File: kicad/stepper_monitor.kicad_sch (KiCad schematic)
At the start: 53 parts, among them J1 Conn_01x04_Male, J2 Conn_01x04_Male, J3 Conn_01x02_Male, J4 USB_C_Receptacle_USB2.0, J5 JTAG, M1 Motor-simple_stepper_motor_an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, Q1 UMH3N, Q2 PJA3439, SW1 SW_Push, U1 CP2102N-A01-GQFN28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

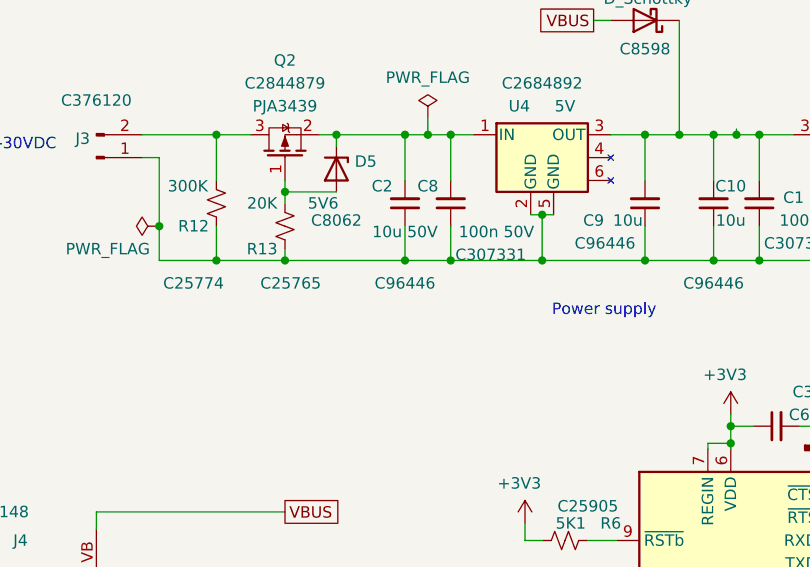
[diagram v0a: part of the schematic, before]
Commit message: Cleaned up the PCB layout.
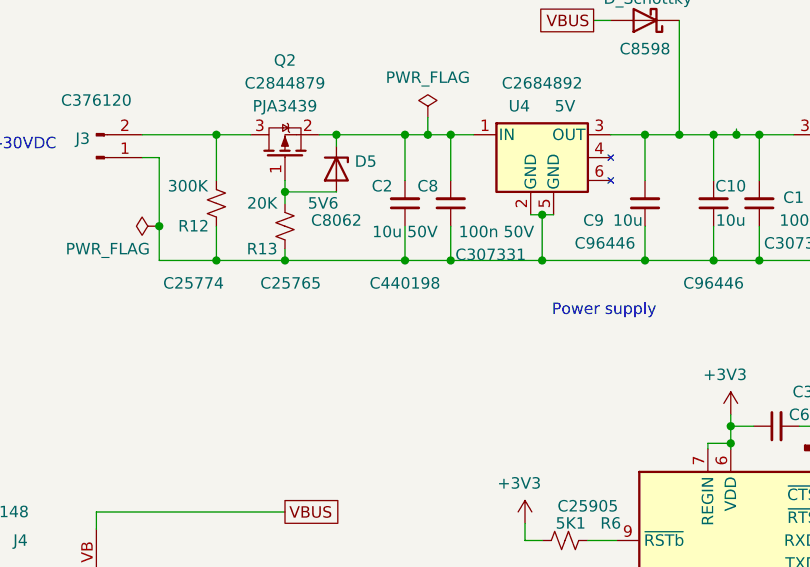
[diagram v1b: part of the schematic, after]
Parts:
- C10, C16, C3, C9: footprint Capacitor_SMD:C_0402_1005Metric -> Capacitor_SMD:C_0603_1608Metric
- C2: footprint Capacitor_SMD:C_0402_1005Metric -> Capacitor_SMD:C_0805_2012Metric; LCSC C96446 -> C440198
- Q2: footprint Package_TO_SOT_SMD:SOT-23 -> stepper_monitor:SOT-23
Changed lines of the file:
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@@
     (property "Reference" "C3" (id 0) (at 126.365 43.18 0))
     (property "Value" "10u" (id 1) (at 126.365 46.99 0))
-    (property "Footprint" "Capacitor_SMD:C_0402_1005Metric" (id 2) (at 128.27 45.085 0)
+    (property "Footprint" "Capacitor_SMD:C_0603_1608Metric" (id 2) (at 128.27 45.085 0)
       (effects (font (size 1.27 1.27)) hide)
     )
@@
     (property "Reference" "C10" (id 0) (at 103.505 43.18 0))
     (property "Value" "10u" (id 1) (at 103.505 46.99 0))
-    (property "Footprint" "Capacitor_SMD:C_0402_1005Metric" (id 2) (at 101.6 45.085 0)
+    (property "Footprint" "Capacitor_SMD:C_0603_1608Metric" (id 2) (at 101.6 45.085 0)
       (effects (font (size 1.27 1.27)) hide)
     )
@@
     (property "Reference" "C2" (id 0) (at 64.77 43.18 0))
     (property "Value" "10u 50V" (id 1) (at 67.31 48.26 0))
-    (property "Footprint" "Capacitor_SMD:C_0402_1005Metric" (id 2) (at 67.31 45.085 0)
+    (property "Footprint" "Capacitor_SMD:C_0805_2012Metric" (id 2) (at 67.31 45.085 0)
       (effects (font (size 1.27 1.27)) hide)
     )
@@
       (effects (font (size 1.27 1.27)) hide)
     )
-    (property "LCSC" "C96446" (id 4) (at 67.31 53.975 0))
+    (property "LCSC" "C440198" (id 4) (at 67.31 53.975 0))
     (pin "1")
     (pin "2")
@@
     (property "Reference" "Q2" (id 0) (at 53.975 29.21 90))
     (property "Value" "PJA3439" (id 1) (at 53.975 34.29 90))
-    (property "Footprint" "Package_TO_SOT_SMD:SOT-23" (id 2) (at 55.88 34.925 0)
+    (property "Footprint" "stepper_monitor:SOT-23" (id 2) (at 55.88 34.925 0)
       (effects (font (size 1.27 1.27) italic) (justify left) hide)
     )
@@
     (property "Reference" "C16" (id 0) (at 205.74 29.845 0))
     (property "Value" "10u" (id 1) (at 205.74 31.75 0))
-    (property "Footprint" "Capacitor_SMD:C_0402_1005Metric" (id 2) (at 209.55 30.48 0)
+    (property "Footprint" "Capacitor_SMD:C_0603_1608Metric" (id 2) (at 209.55 30.48 0)
       (effects (font (size 1.27 1.27)) hide)
     )
@@
     (property "Reference" "C9" (id 0) (at 88.265 46.99 0))
     (property "Value" "10u" (id 1) (at 92.075 46.99 0))
-    (property "Footprint" "Capacitor_SMD:C_0402_1005Metric" (id 2) (at 93.98 45.085 0)
+    (property "Footprint" "Capacitor_SMD:C_0603_1608Metric" (id 2) (at 93.98 45.085 0)
       (effects (font (size 1.27 1.27)) hide)
     )
@@
     )
     (path "/218e73b4-d1ff-4eed-a2d4-42d93c5c0f72"
-      (reference "C2") (unit 1) (value "10u 50V") (footprint "Capacitor_SMD:C_0402_1005Metric")
+      (reference "C2") (unit 1) (value "10u 50V") (footprint "Capacitor_SMD:C_0805_2012Metric")
     )
     (path "/00000000-0000-0000-0000-00006317d8b3"
-      (reference "C3") (unit 1) (value "10u") (footprint "Capacitor_SMD:C_0402_1005Metric")
+      (reference "C3") (unit 1) (value "10u") (footprint "Capacitor_SMD:C_0603_1608Metric")
     )
     (path "/00000000-0000-0000-0000-000063186d0f"
@@
     )
     (path "/cb4273f4-9404-4fd5-bce3-443a59d164e3"
-      (reference "C9") (unit 1) (value "10u") (footprint "Capacitor_SMD:C_0402_1005Metric")
+      (reference "C9") (unit 1) (value "10u") (footprint "Capacitor_SMD:C_0603_1608Metric")
     )
     (path "/093765e9-ac92-428d-96f2-1ae287fc4af6"
-      (reference "C10") (unit 1) (value "10u") (footprint "Capacitor_SMD:C_0402_1005Metric")
+      (reference "C10") (unit 1) (value "10u") (footprint "Capacitor_SMD:C_0603_1608Metric")
     )
     (path "/9ce3787c-7546-4e46-9b55-aaf3ff59b639"
@@
     )
     (path "/bc1a567a-82f7-43c3-b7d6-54c2aa341a86"
-      (reference "C16") (unit 1) (value "10u") (footprint "Capacitor_SMD:C_0402_1005Metric")
+      (reference "C16") (unit 1) (value "10u") (footprint "Capacitor_SMD:C_0603_1608Metric")
     )
     (path "/00000000-0000-0000-0000-00006319144c"
@@
     )
     (path "/420a49fa-bc07-40b0-8b18-684ba9455b7a"
-      (reference "Q2") (unit 1) (value "PJA3439") (footprint "Package_TO_SOT_SMD:SOT-23")
+      (reference "Q2") (unit 1) (value "PJA3439") (footprint "stepper_monitor:SOT-23")
     )
     (path "/00000000-0000-0000-0000-000063145bc1"

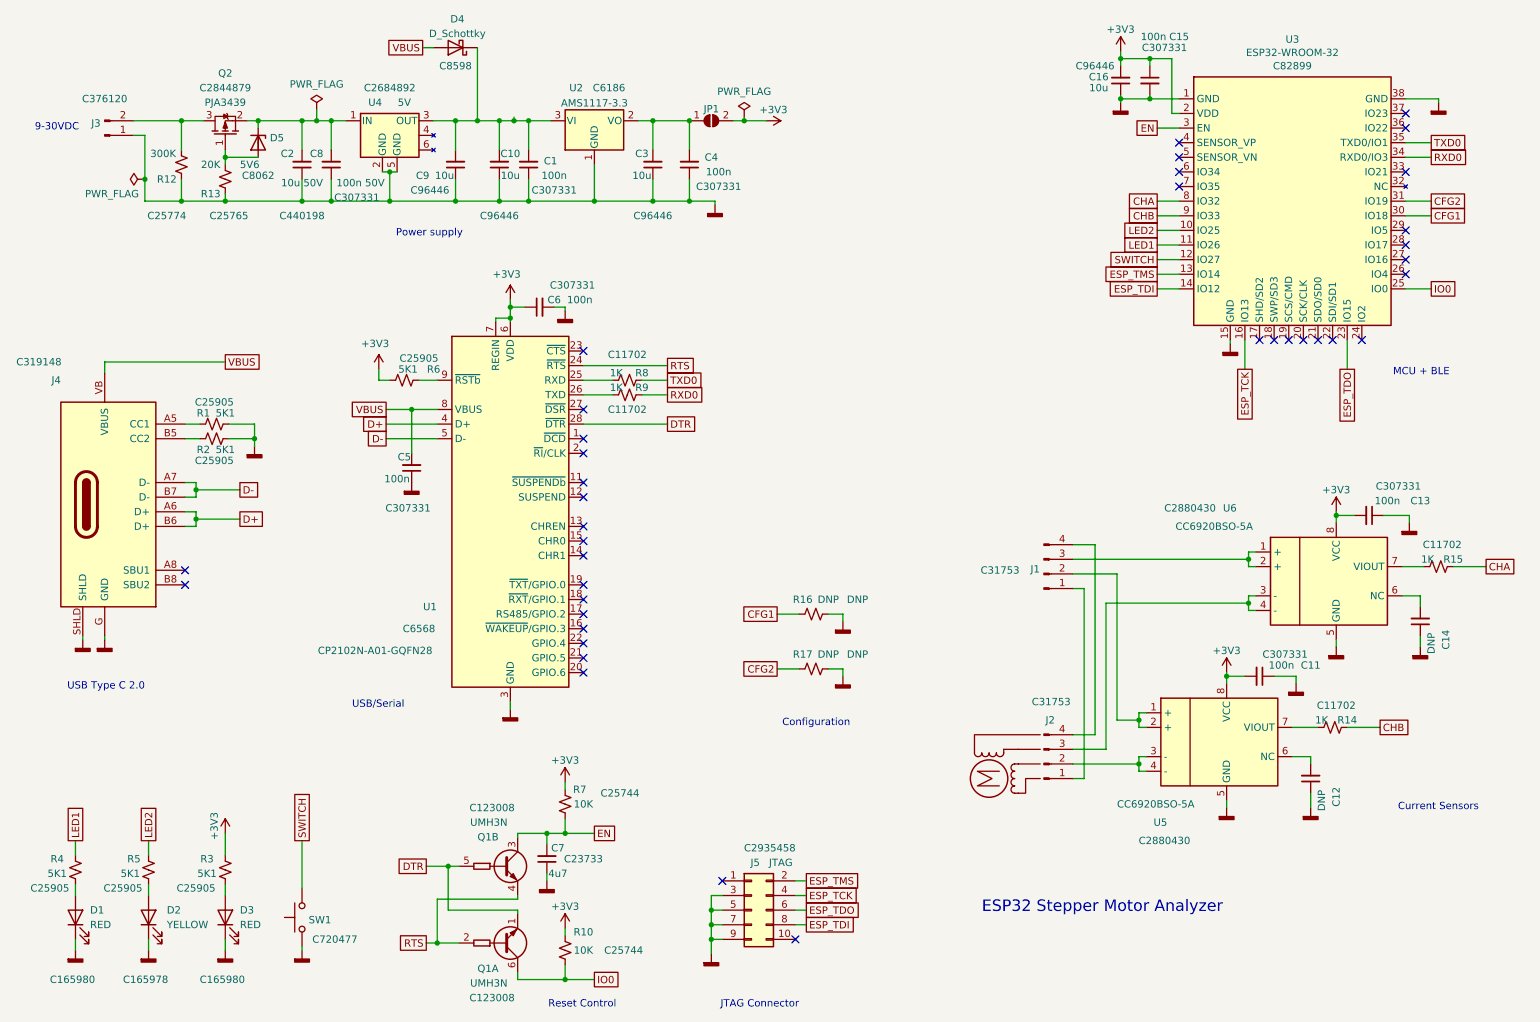
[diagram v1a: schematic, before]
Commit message: Minor PCB layout tweaks.
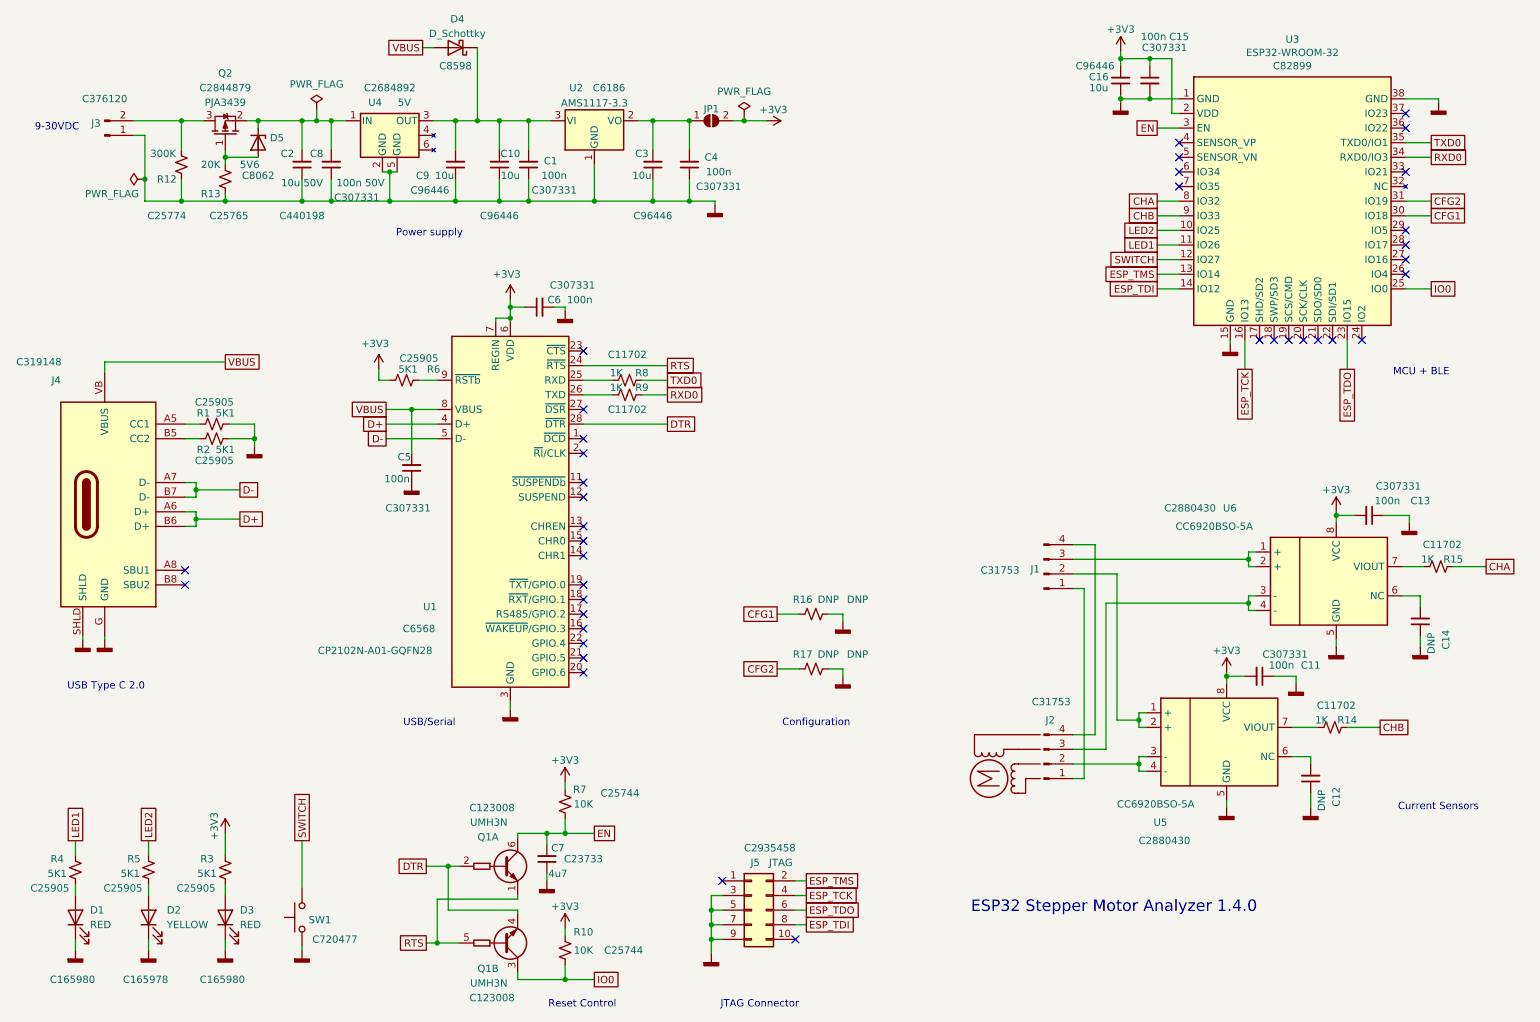
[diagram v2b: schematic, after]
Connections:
- net DTR: now also Q1.2 (B1), Q1.4 (E2); no longer Q1.1 (E1), Q1.5 (B2)
- net EN: now also Q1.6 (C1); no longer Q1.3 (C2)
- net IO0: now also Q1.3 (C2); no longer Q1.6 (C1)
- net RTS: now also Q1.1 (E1), Q1.5 (B2); no longer Q1.2 (B1), Q1.4 (E2)
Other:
- note added: "ESP32 Stepper Motor Analyzer 1.4.0"
- note removed: "ESP32 Stepper Motor Analyzer"
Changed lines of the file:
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@@
   (junction (at 231.775 121.285) (diameter 0) (color 0 0 0 0)
-  )
-  (junction (at 104.14 37.465) (diameter 0) (color 0 0 0 0)
   )
   (junction (at 82.55 51.435) (diameter 0) (color 0 0 0 0)
@@
     (stroke (width 0) (type default) (color 0 0 0 0))
   )
-  (wire (pts (xy 101.6 37.465) (xy 104.14 37.465))
+  (wire (pts (xy 101.6 37.465) (xy 106.68 37.465))
     (stroke (width 0) (type default) (color 0 0 0 0))
   )
@@
     (stroke (width 0) (type default) (color 0 0 0 0))
   )
-  (wire (pts (xy 104.14 36.83) (xy 104.14 37.465))
-    (stroke (width 0) (type default) (color 0 0 0 0))
-  )
   (wire (pts (xy 109.855 161.29) (xy 113.03 161.29))
     (stroke (width 0) (type default) (color 0 0 0 0))
@@
   )
   (wire (pts (xy 259.08 41.275) (xy 263.525 41.275))
-    (stroke (width 0) (type default) (color 0 0 0 0))
-  )
-  (wire (pts (xy 104.14 37.465) (xy 106.68 37.465))
     (stroke (width 0) (type default) (color 0 0 0 0))
   )
@@
     (effects (font (size 1.27 1.27)) (justify right bottom))
   )
-  (text "USB/Serial" (at 85.09 139.7 180)
+  (text "USB/Serial" (at 93.98 142.875 180)
     (effects (font (size 1.27 1.27)) (justify right bottom))
   )
@@
     (effects (font (size 1.27 1.27)) (justify right bottom))
   )
-  (text "ESP32 Stepper Motor Analyzer" (at 227.33 175.26 180)
-    (effects (font (size 2 2)) (justify right bottom))
+  (text "ESP32 Stepper Motor Analyzer 1.4.0" (at 183.515 175.26 0)
+    (effects (font (size 2 2)) (justify left bottom))
   )
   (global_label "ESP_TDO" (shape passive) (at 248.92 80.645 270) (fields_autoplaced)
@@
     (pin "8")
   )
-  (symbol (lib_id "Transistor_BJT:UMH3N") (at 99.695 167.005 0) (unit 2)
+  (symbol (lib_id "Transistor_BJT:UMH3N") (at 99.695 167.005 0) (unit 1)
     (in_bom yes) (on_board yes)
     (property "Reference" "Q1" (id 0) (at 97.79 161.925 0)
@@
     (pin "4")
   )
-  (symbol (lib_id "Transistor_BJT:UMH3N") (at 99.695 180.34 0) (mirror x) (unit 1)
+  (symbol (lib_id "Transistor_BJT:UMH3N") (at 99.695 180.34 0) (mirror x) (unit 2)
     (in_bom yes) (on_board yes)
     (property "Reference" "Q1" (id 0) (at 97.79 184.785 0)
@@
       (reference "M1") (unit 1) (value "Motor-simple_stepper_motor_analyzer") (footprint "stepper_monitor:Empty")
     )
+    (path "/972e7b42-d79f-4e43-9830-0a496a349e58"
+      (reference "Q1") (unit 1) (value "UMH3N") (footprint "stepper_monitor:SOT-363_SC-70-6")
+    )
     (path "/f1fd41ef-85ac-46c3-976e-cf8236d850dc"
-      (reference "Q1") (unit 1) (value "UMH3N") (footprint "stepper_monitor:SOT-363_SC-70-6")
-    )
-    (path "/972e7b42-d79f-4e43-9830-0a496a349e58"
       (reference "Q1") (unit 2) (value "UMH3N") (footprint "stepper_monitor:SOT-363_SC-70-6")
     )

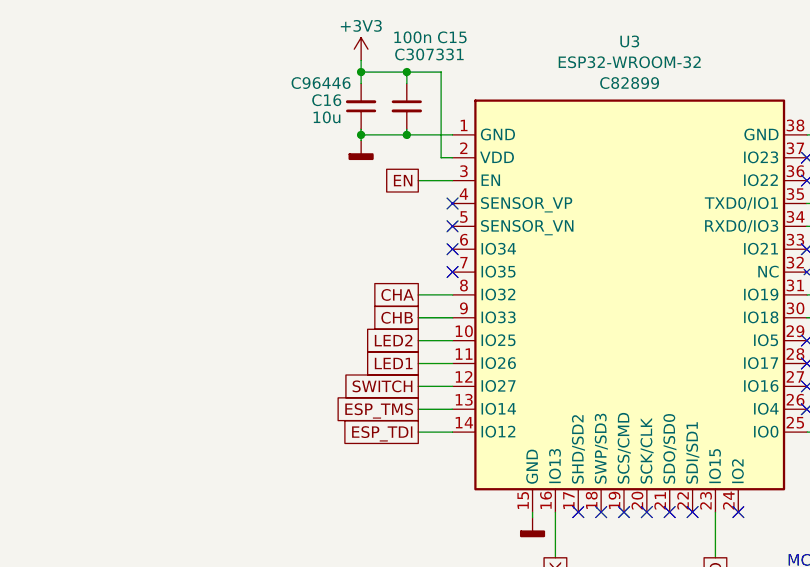
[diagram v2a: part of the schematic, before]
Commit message: Updated analog input pins.
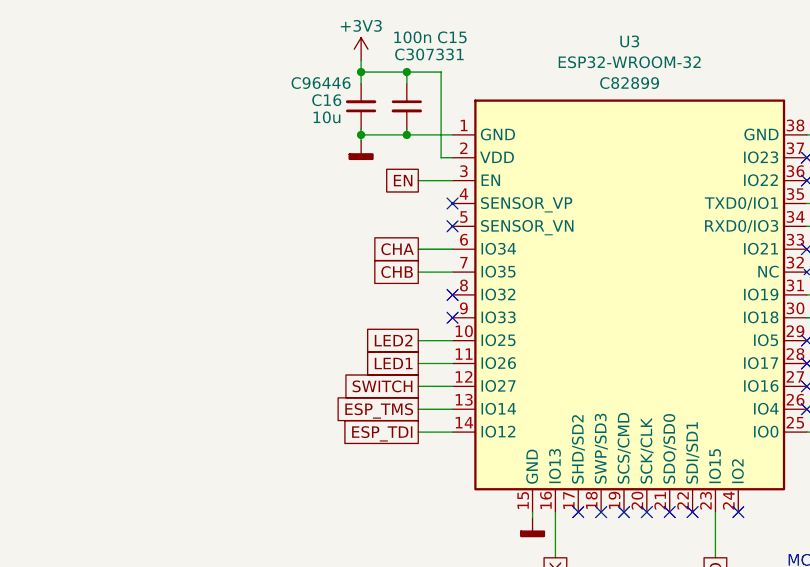
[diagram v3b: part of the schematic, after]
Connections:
- net CHA: now also U3.6 (IO34); no longer U3.8 (IO32)
- net CHB: now also U3.7 (IO35); no longer U3.9 (IO33)
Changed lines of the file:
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@@
   (junction (at 86.36 87.63) (diameter 0) (color 0 0 0 0)
   )
-  (no_connect (at 219.71 48.895))
   (no_connect (at 219.71 41.275))
   (no_connect (at 219.71 43.815))
-  (no_connect (at 219.71 46.355))
   (no_connect (at 233.68 75.565))
   (no_connect (at 236.22 75.565))
@@
   (no_connect (at 116.205 125.73))
   (no_connect (at 116.205 123.19))
+  (no_connect (at 219.71 53.975))
+  (no_connect (at 219.71 51.435))
   (no_connect (at 116.205 95.25))
   (no_connect (at 116.205 128.27))
@@
     (stroke (width 0) (type default) (color 0 0 0 0))
   )
+  (wire (pts (xy 215.9 48.895) (xy 219.71 48.895))
+    (stroke (width 0) (type default) (color 0 0 0 0))
+  )
   (wire (pts (xy 201.295 151.765) (xy 203.2 151.765))
     (stroke (width 0) (type default) (color 0 0 0 0))
@@
     (stroke (width 0) (type default) (color 0 0 0 0))
   )
+  (wire (pts (xy 215.9 46.355) (xy 219.71 46.355))
+    (stroke (width 0) (type default) (color 0 0 0 0))
+  )
   (wire (pts (xy 81.915 87.63) (xy 86.36 87.63))
     (stroke (width 0) (type default) (color 0 0 0 0))
@@
     (stroke (width 0) (type default) (color 0 0 0 0))
   )
-  (wire (pts (xy 215.9 51.435) (xy 219.71 51.435))
-    (stroke (width 0) (type default) (color 0 0 0 0))
-  )
   (wire (pts (xy 219.71 56.515) (xy 215.9 56.515))
     (stroke (width 0) (type default) (color 0 0 0 0))
@@
   )
   (wire (pts (xy 40.005 47.625) (xy 40.005 51.435))
-    (stroke (width 0) (type default) (color 0 0 0 0))
-  )
-  (wire (pts (xy 215.9 53.975) (xy 219.71 53.975))
     (stroke (width 0) (type default) (color 0 0 0 0))
   )
@@
     )
   )
-  (global_label "CHB" (shape passive) (at 215.9 53.975 180) (fields_autoplaced)
-    (effects (font (size 1.27 1.27)) (justify right))
-    (property "Intersheet References" "${INTERSHEET_REFS}" (id 0) (at 209.7053 53.8956 0)
+  (global_label "CHB" (shape passive) (at 215.9 48.895 180) (fields_autoplaced)
+    (effects (font (size 1.27 1.27)) (justify right))
+    (property "Intersheet References" "${INTERSHEET_REFS}" (id 0) (at 209.7053 48.8156 0)
       (effects (font (size 1.27 1.27)) (justify right) hide)
     )
@@
     )
   )
-  (global_label "CHA" (shape passive) (at 215.9 51.435 180) (fields_autoplaced)
-    (effects (font (size 1.27 1.27)) (justify right))
-    (property "Intersheet References" "${INTERSHEET_REFS}" (id 0) (at 209.8868 51.3556 0)
-      (effects (font (size 1.27 1.27)) (justify right) hide)
-    )
+  (global_label "CHA" (shape passive) (at 215.9 46.355 180) (fields_autoplaced)
+    (effects (font (size 1.27 1.27)) (justify right))
+    (property "Intersheet References" "${INTERSHEET_REFS}" (id 0) (at 209.8868 46.2756 0)
+      (effects (font (size 1.27 1.27)) (justify right) hide)
+    )
